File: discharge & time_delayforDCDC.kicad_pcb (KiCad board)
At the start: 2 copper layers, 64.8 x 51 mm, 18 parts, among them J1 43650-0400, J3 43650-0400, J5 43650-0200, J6 43650-0200, K1 DBT71205U, U1 LM393

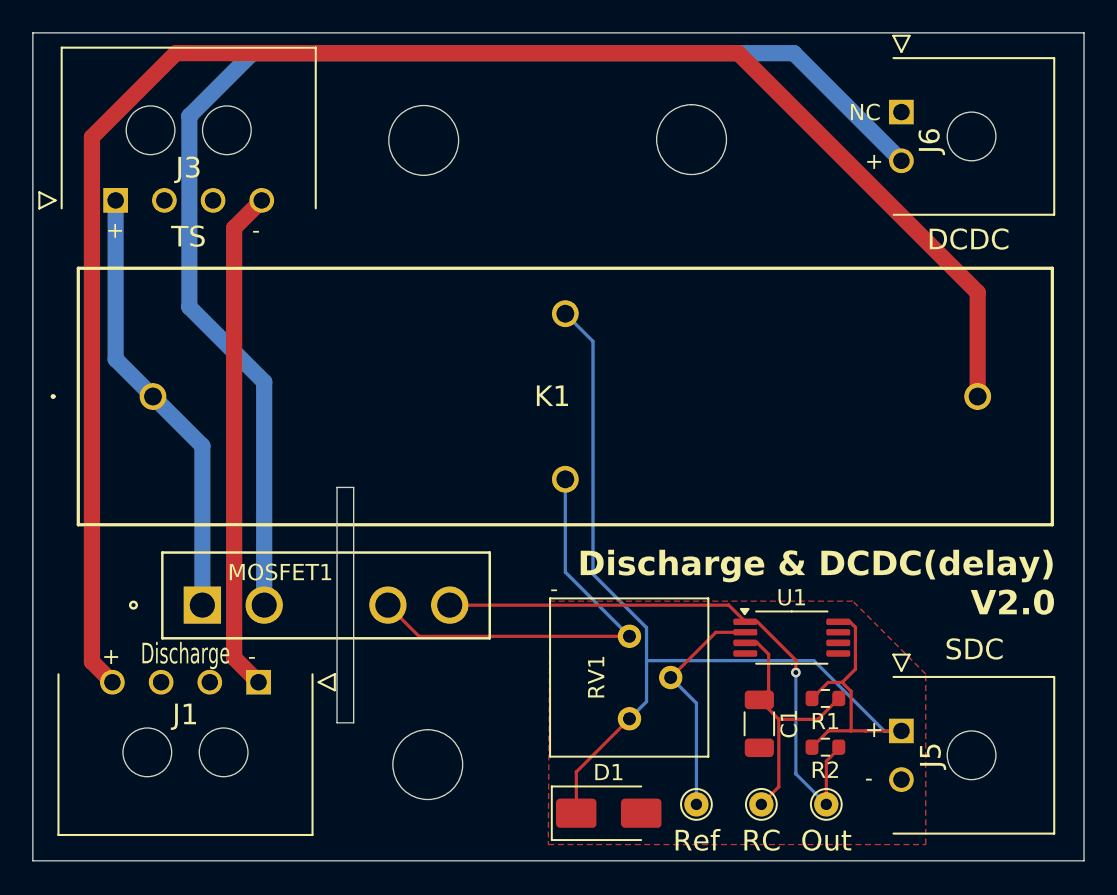
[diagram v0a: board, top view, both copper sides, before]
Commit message: Update schematic and PCB
- Modified properties of test points to exclude from simulation and removed from BOM
- Fix wrong rating of the capacitor
- Updated footprint
- Updated image file
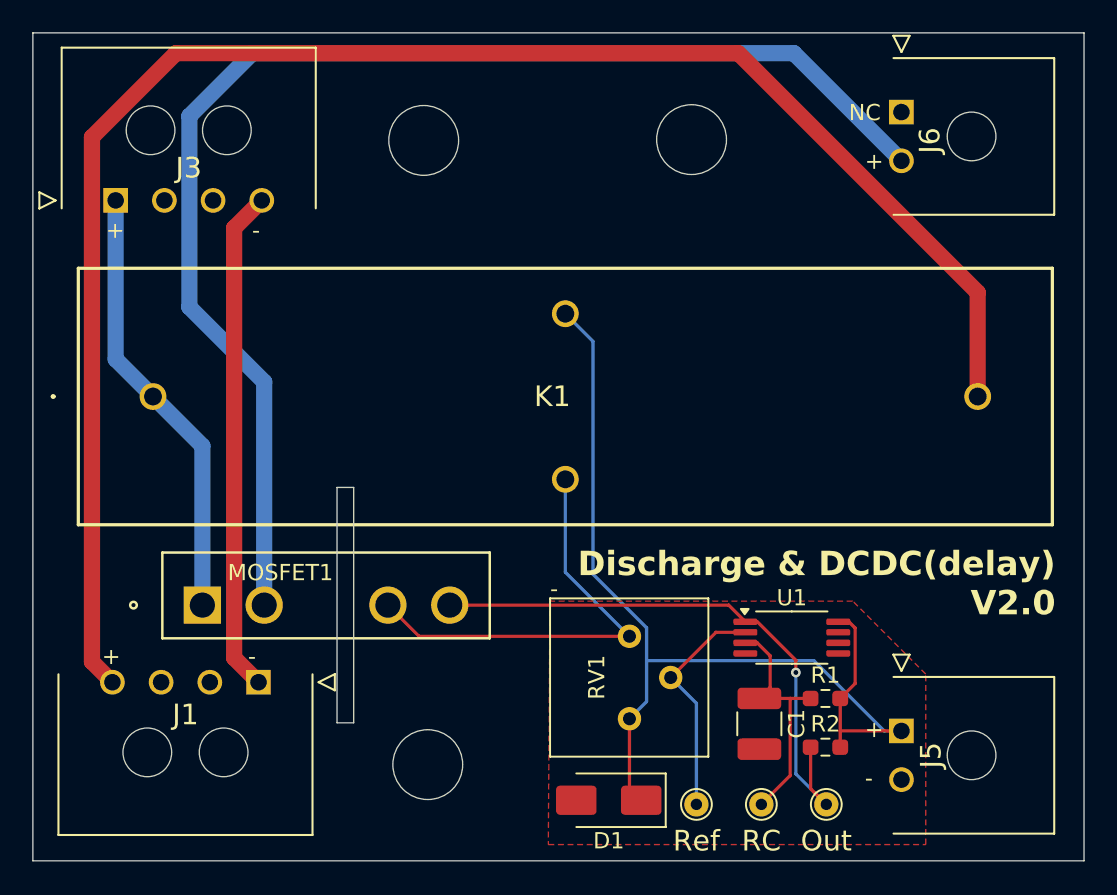
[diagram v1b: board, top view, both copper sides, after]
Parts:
- C1: footprint Capacitor_SMD:C_1206_3216Metric -> Capacitor_SMD:C_1210_3225Metric_Pad1.33x2.70mm_HandSolder
- R1, R2: footprint Resistor_SMD:R_0603_1608Metric -> Resistor_SMD:R_0603_1608Metric_Pad0.98x0.95mm_HandSolder
- moved D1 0.80 mm to (147.2, 125.3), turned to 180 degrees
- turned R1 to 0 degrees
- turned R2 to 0 degrees
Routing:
- net SDC: track 68.5 -> 63.0 mm
- net /Delay: track 16.4 -> 15.2 mm
- net GND: track 27.8 -> 27.0 mm
